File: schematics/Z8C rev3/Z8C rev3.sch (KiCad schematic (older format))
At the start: 0 parts

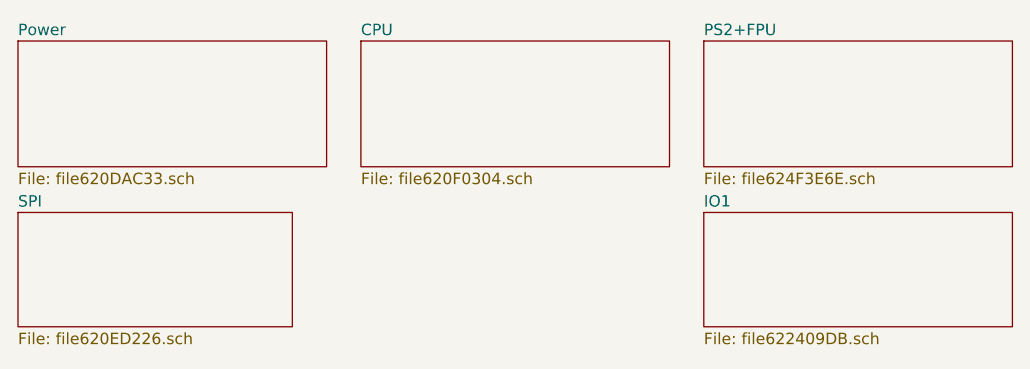
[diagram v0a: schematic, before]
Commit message: working on sound
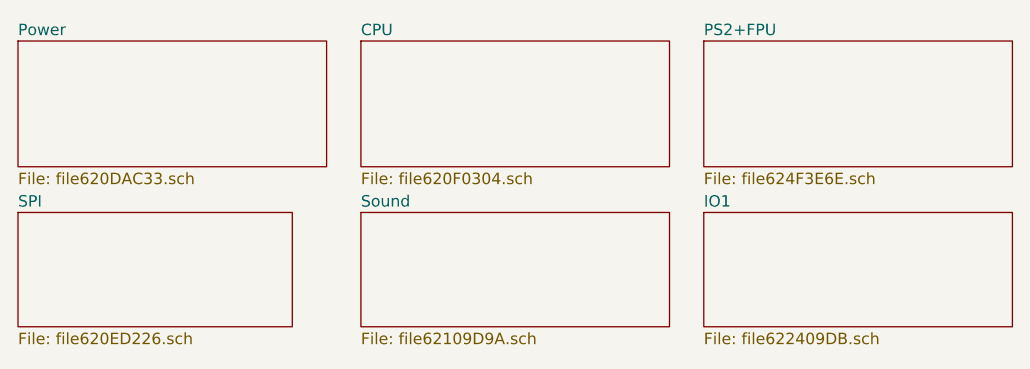
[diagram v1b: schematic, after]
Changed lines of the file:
@@
 $Descr A4 11693 8268
 encoding utf-8
-Sheet 1 6
+Sheet 1 7
 Title "Z8C Homebrew Z80 Computer"
 Date ""
@@
 F1 "file624F3E6E.sch" 50
 $EndSheet
+$Sheet
+S 4250 1550 1350 500
+U 62109D9B
+F0 "Sound" 50
+F1 "file62109D9A.sch" 50
+$EndSheet
 $EndSCHEMATC

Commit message: added bank switching, apu, dma and IRQ logic. Misc. improvements
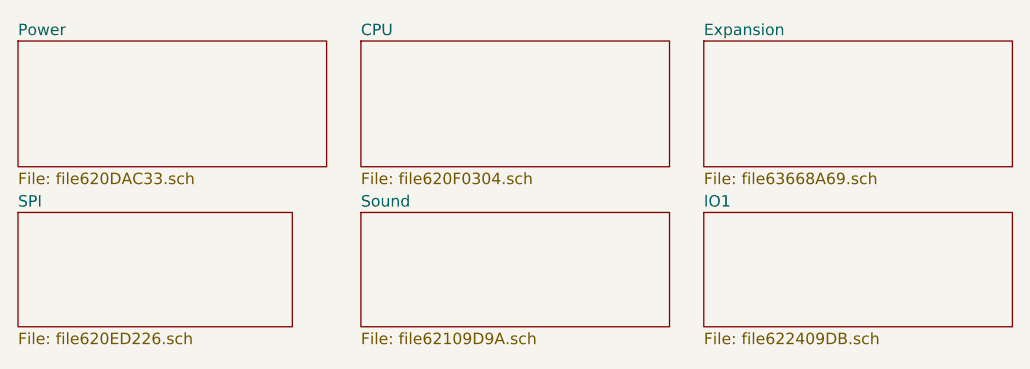
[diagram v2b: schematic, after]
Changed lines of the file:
@@
-$EndSheet
-$Sheet
-S 5750 800  1350 550
-U 624F3E6F
-F0 "PS2+FPU" 50
-F1 "file624F3E6E.sch" 50
 $EndSheet
 $Sheet
@@
 F1 "file62109D9A.sch" 50
 $EndSheet
+$Sheet
+S 5750 800  1350 550
+U 63668A6A
+F0 "Expansion" 50
+F1 "file63668A69.sch" 50
+$EndSheet
 $EndSCHEMATC
